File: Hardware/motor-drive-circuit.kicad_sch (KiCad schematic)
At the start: 13 parts, among them M2 Drive Motor, Q1 IRF540N, Q2 IRF9540N, Q3 IRLZ44N, Q4 IRF40DM229, Q5 IRF9540N, Q6 IRF540N

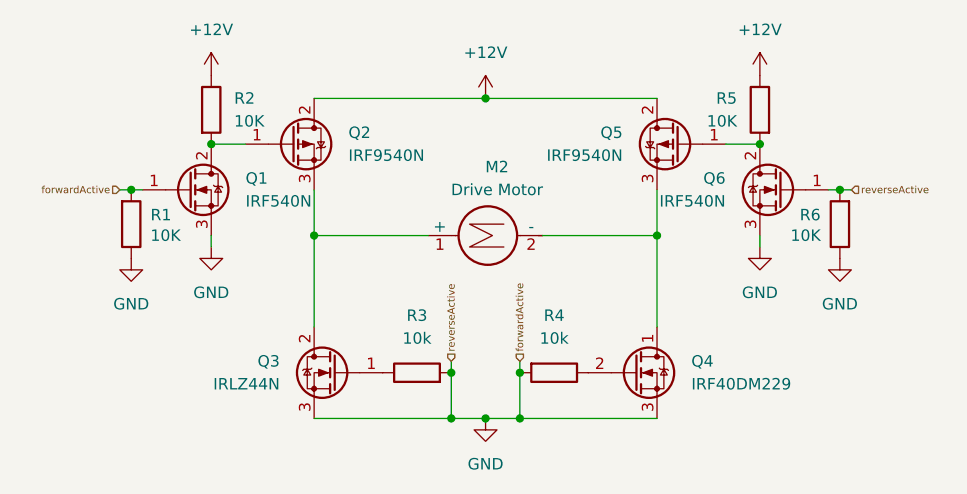
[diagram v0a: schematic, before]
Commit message: fix: mosfet orientation
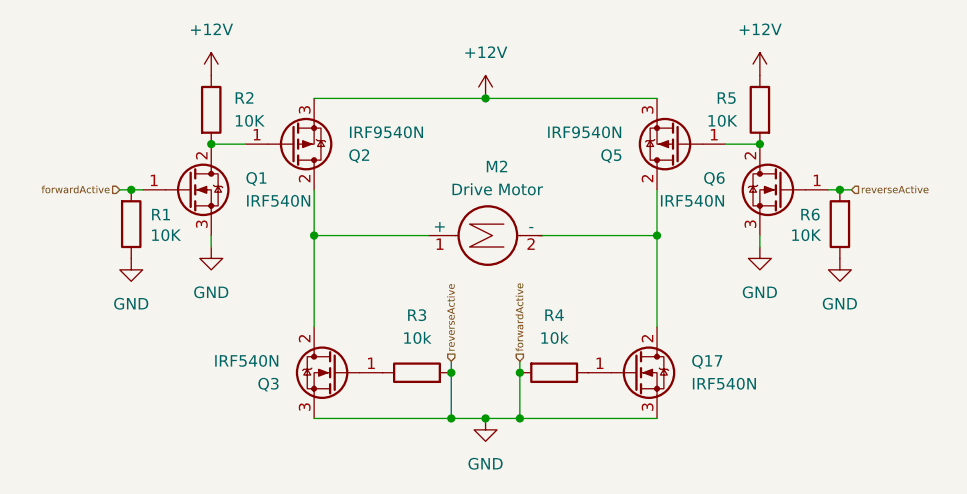
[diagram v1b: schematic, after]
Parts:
- removed Q3: IRLZ44N, Package_DirectFET:DirectFET_MX, symbol Transistor_FET:IRLZ44N
- removed Q4: IRF40DM229, Package_DirectFET:DirectFET_MF, symbol Transistor_FET:IRF40DM229
- added Q17, Q3: IRF540N, Package_TO_SOT_THT:TO-220-3_Vertical, symbol Transistor_FET:IRF540N
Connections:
- net +12V: now also Q2.3 (S), Q5.3 (S); no longer Q2.2 (D), Q5.2 (D)
- net GND: now also Q17.3 (S), Q3.3 (S)
- net at R4.1: now also Q17.1 (G)
- net at M2.2 (-): now also Q5.2 (D), Q17.2 (D); no longer Q5.3 (S)
- net at M2.1 (+): now also Q2.2 (D), Q3.2 (D); no longer Q2.3 (S)
- net at R3.1: now also Q3.1 (G)
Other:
- moved on the sheet: Q5
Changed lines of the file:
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@@
-	)
-	(symbol
-		(lib_id "Transistor_FET:IRF40DM229")
-		(at 156.21 109.22 0)
-		(unit 1)
-		(exclude_from_sim no)
-		(in_bom yes)
-		(on_board yes)
-		(dnp no)
-		(fields_autoplaced yes)
-		(property "Reference" "Q4"
-			(at 162.56 107.9499 0)
-			(effects
-				(font
-					(size 1.27 1.27)
-				)
-				(justify left)
-			)
-		)
-		(property "Value" "IRF40DM229"
-			(at 162.56 110.4899 0)
-			(effects
-				(font
-					(size 1.27 1.27)
-				)
-				(justify left)
-			)
-		)
-		(property "Footprint" "Package_DirectFET:DirectFET_MF"
-			(at 161.29 111.125 0)
-			(effects
-				(font
-					(size 1.27 1.27)
-					(italic yes)
-				)
-				(justify left)
-				(hide yes)
-			)
-		)
-		(property "Datasheet" "https://www.infineon.com/dgdl/Infineon-IRF40DM229-DS-v02_00-EN.pdf?fileId=5546d462557e6e890155a15c899160ea"
-			(at 161.29 113.03 0)
-			(effects
-				(font
-					(size 1.27 1.27)
-				)
-				(justify left)
-				(hide yes)
-			)
-		)
-		(property "Description" "159A Id, 40V Vds, 1.85mOhm Rds, N-Channel MOSFET, DirectFET MF"
-			(at 156.21 109.22 0)
-			(effects
-				(font
-					(size 1.27 1.27)
-				)
-				(hide yes)
-			)
-		)
-		(pin "2"
-		)
-		(pin "1"
-		)
-		(pin "3"
-		)
-		(instances
-			(project "OpenVac"
-				(path "/cfb1a53c-1978-4730-a380-294525b876d3/491fb852-02ab-46ec-8569-0a07edbc390f"
-					(reference "Q4")
-					(unit 1)
-				)
-				(path "/cfb1a53c-1978-4730-a380-294525b876d3/08f6c6d2-33d9-4f58-9cda-ca1b9dcb0eee"
-					(reference "Q14")
-					(unit 1)
-				)
-			)
-		)
 	)
 	(symbol
@@
 	(symbol
 		(lib_id "Transistor_FET:IRF9540N")
-		(at 161.29 83.82 0)
-		(mirror y)
+		(at 161.29 83.82 180)
 		(unit 1)
 		(exclude_from_sim no)
@@
 		(dnp no)
 		(property "Reference" "Q5"
-			(at 154.94 82.5499 0)
+			(at 154.94 85.0901 0)
 			(effects
 				(font
@@
 		)
 		(property "Value" "IRF9540N"
-			(at 154.94 85.0899 0)
+			(at 154.94 82.5501 0)
 			(effects
 				(font
@@
 		)
 		(property "Footprint" "Package_TO_SOT_THT:TO-220-3_Vertical"
-			(at 156.21 85.725 0)
+			(at 156.21 81.915 0)
 			(effects
 				(font
@@
 		)
 		(property "Datasheet" "http://www.irf.com/product-info/datasheets/data/irf9540n.pdf"
-			(at 156.21 87.63 0)
+			(at 156.21 80.01 0)
 			(effects
 				(font
@@
 		(lib_id "Transistor_FET:IRF9540N")
 		(at 118.11 83.82 0)
-		(unit 1)
-		(exclude_from_sim no)
-		(in_bom yes)
-		(on_board yes)
-		(dnp no)
-		(fields_autoplaced yes)
+		(mirror x)
+		(unit 1)
+		(exclude_from_sim no)
+		(in_bom yes)
+		(on_board yes)
+		(dnp no)
 		(property "Reference" "Q2"
-			(at 124.46 82.5499 0)
+			(at 124.46 85.0901 0)
 			(effects
 				(font
@@
 		)
 		(property "Value" "IRF9540N"
-			(at 124.46 85.0899 0)
+			(at 124.46 82.5501 0)
 			(effects
 				(font
@@
 		)
 		(property "Footprint" "Package_TO_SOT_THT:TO-220-3_Vertical"
-			(at 123.19 85.725 0)
+			(at 123.19 81.915 0)
 			(effects
 				(font
@@
 		)
 		(property "Datasheet" "http://www.irf.com/product-info/datasheets/data/irf9540n.pdf"
-			(at 123.19 87.63 0)
+			(at 123.19 80.01 0)
 			(effects
 				(font
@@
 	)
 	(symbol
-		(lib_id "Transistor_FET:IRLZ44N")
+		(lib_id "Transistor_FET:IRF540N")
+		(at 156.21 109.22 0)
+		(unit 1)
+		(exclude_from_sim no)
+		(in_bom yes)
+		(on_board yes)
+		(dnp no)
+		(property "Reference" "Q17"
+			(at 162.56 107.9499 0)
+			(effects
+				(font
+					(size 1.27 1.27)
+				)
+				(justify left)
+			)
+		)
+		(property "Value" "IRF540N"
+			(at 162.56 110.4899 0)
+			(effects
+				(font
+					(size 1.27 1.27)
+				)
+				(justify left)
+			)
+		)
+		(property "Footprint" "Package_TO_SOT_THT:TO-220-3_Vertical"
+			(at 161.29 111.125 0)
+			(effects
+				(font
+					(size 1.27 1.27)
+					(italic yes)
+				)
+				(justify left)
+				(hide yes)
+			)
+		)
+		(property "Datasheet" "http://www.irf.com/product-info/datasheets/data/irf540n.pdf"
+			(at 161.29 113.03 0)
+			(effects
+				(font
+					(size 1.27 1.27)
+				)
+				(justify left)
+				(hide yes)
+			)
+		)
+		(property "Description" "33A Id, 100V Vds, HEXFET N-Channel MOSFET, TO-220"
+			(at 156.21 109.22 0)
+			(effects
+				(font
+					(size 1.27 1.27)
+				)
+				(hide yes)
+			)
+		)
+		(pin "1"
+		)
+		(pin "2"
+		)
+		(pin "3"
+		)
+		(instances
+			(project "OpenVac"
+				(path "/cfb1a53c-1978-4730-a380-294525b876d3/491fb852-02ab-46ec-8569-0a07edbc390f"
+					(reference "Q17")
+					(unit 1)
+				)
+				(path "/cfb1a53c-1978-4730-a380-294525b876d3/08f6c6d2-33d9-4f58-9cda-ca1b9dcb0eee"
+					(reference "Q18")
+					(unit 1)
+				)
+			)
+		)
+	)
+	(symbol
+		(lib_id "Transistor_FET:IRF540N")
 		(at 123.19 109.22 0)
 		(mirror y)
@@
 		(dnp no)
 		(property "Reference" "Q3"
-			(at 116.84 107.9499 0)
-			(effects
-				(font
-					(size 1.27 1.27)
-				)
-				(justify left)
-			)
-		)
-		(property "Value" "IRLZ44N"
-			(at 116.84 110.4899 0)
-			(effects
-				(font
-					(size 1.27 1.27)
-				)
-				(justify left)
-			)
-		)
-		(property "Footprint" "Package_DirectFET:DirectFET_MX"
+			(at 116.84 110.4901 0)
+			(effects
+				(font
+					(size 1.27 1.27)
+				)
+				(justify left)
+			)
+		)
+		(property "Value" "IRF540N"
+			(at 116.84 107.9501 0)
+			(effects
+				(font
+					(size 1.27 1.27)
+				)
+				(justify left)
+			)
+		)
+		(property "Footprint" "Package_TO_SOT_THT:TO-220-3_Vertical"
 			(at 118.11 111.125 0)
 			(effects
@@
 			)
 		)
-		(property "Datasheet" "http://www.irf.com/product-info/datasheets/data/irlz44n.pdf"
+		(property "Datasheet" "http://www.irf.com/product-info/datasheets/data/irf540n.pdf"
 			(at 118.11 113.03 0)
 			(effects
@@
 			)
 		)
-		(property "Description" "47A Id, 55V Vds, 22mOhm Rds Single N-Channel HEXFET Power MOSFET, TO-220AB"
+		(property "Description" "33A Id, 100V Vds, HEXFET N-Channel MOSFET, TO-220"
 			(at 123.19 109.22 0)
 			(effects
@@
 			)
 		)
+		(pin "1"
+		)
+		(pin "2"
+		)
 		(pin "3"
 		)
-		(pin "2"
-		)
-		(pin "1"
-		)
 		(instances
 			(project "OpenVac"
@@
 				)
 				(path "/cfb1a53c-1978-4730-a380-294525b876d3/08f6c6d2-33d9-4f58-9cda-ca1b9dcb0eee"
-					(reference "Q13")
-					(unit 1)
-				)
+					(reference "Q4")
+					(unit 1)
+				)

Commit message: Session 13 hardware modifications
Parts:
- renumbered Q1 to Q11, Q2 to Q12, Q5 to Q15, Q6 to Q16, Q17 to Q18, Q3 to Q4, R1 to R19, R2 to R20, R3 to R21, R4 to R22, R5 to R23, R6 to R24
